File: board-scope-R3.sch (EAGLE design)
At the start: 71 parts, among them IC3 STM32F103C8T, J2 632723300011, U1 HD3SS3220IRNHT, U2 TUSB8020B, U3 FT600Q-T, U4 ICE40HX1K-VQ100VQ-100, U5 25F32006WSOI, U7 TPS54386, X1 30Mhz, X2 8Mhz

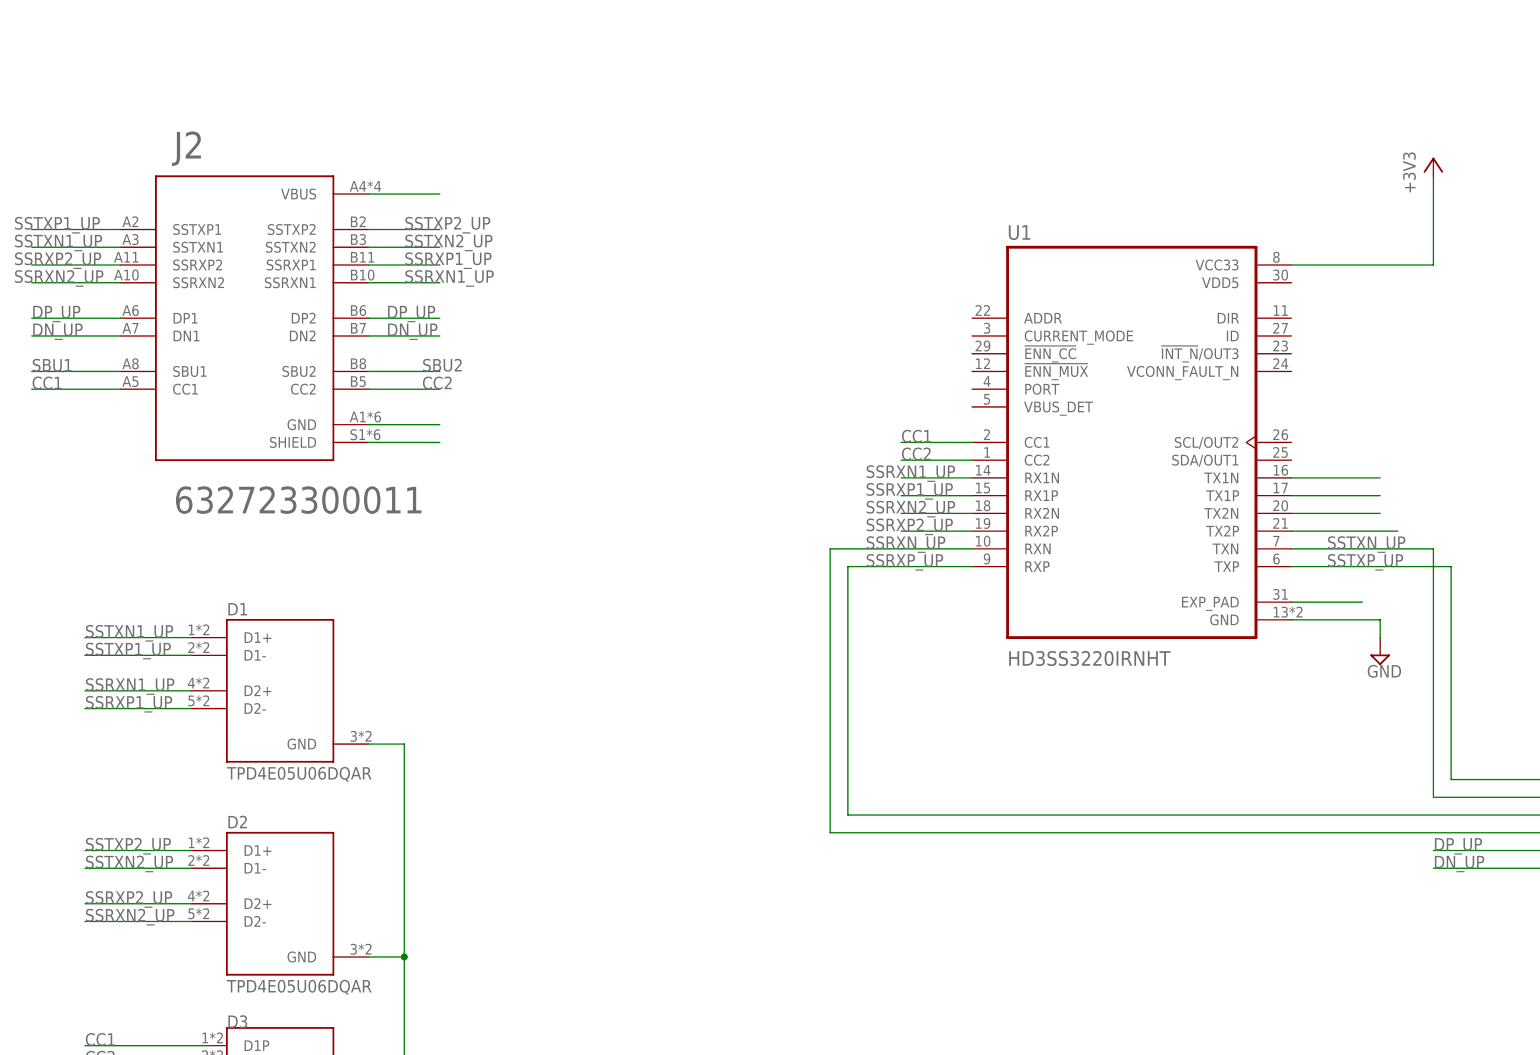
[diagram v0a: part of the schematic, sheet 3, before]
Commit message: routed power and usb
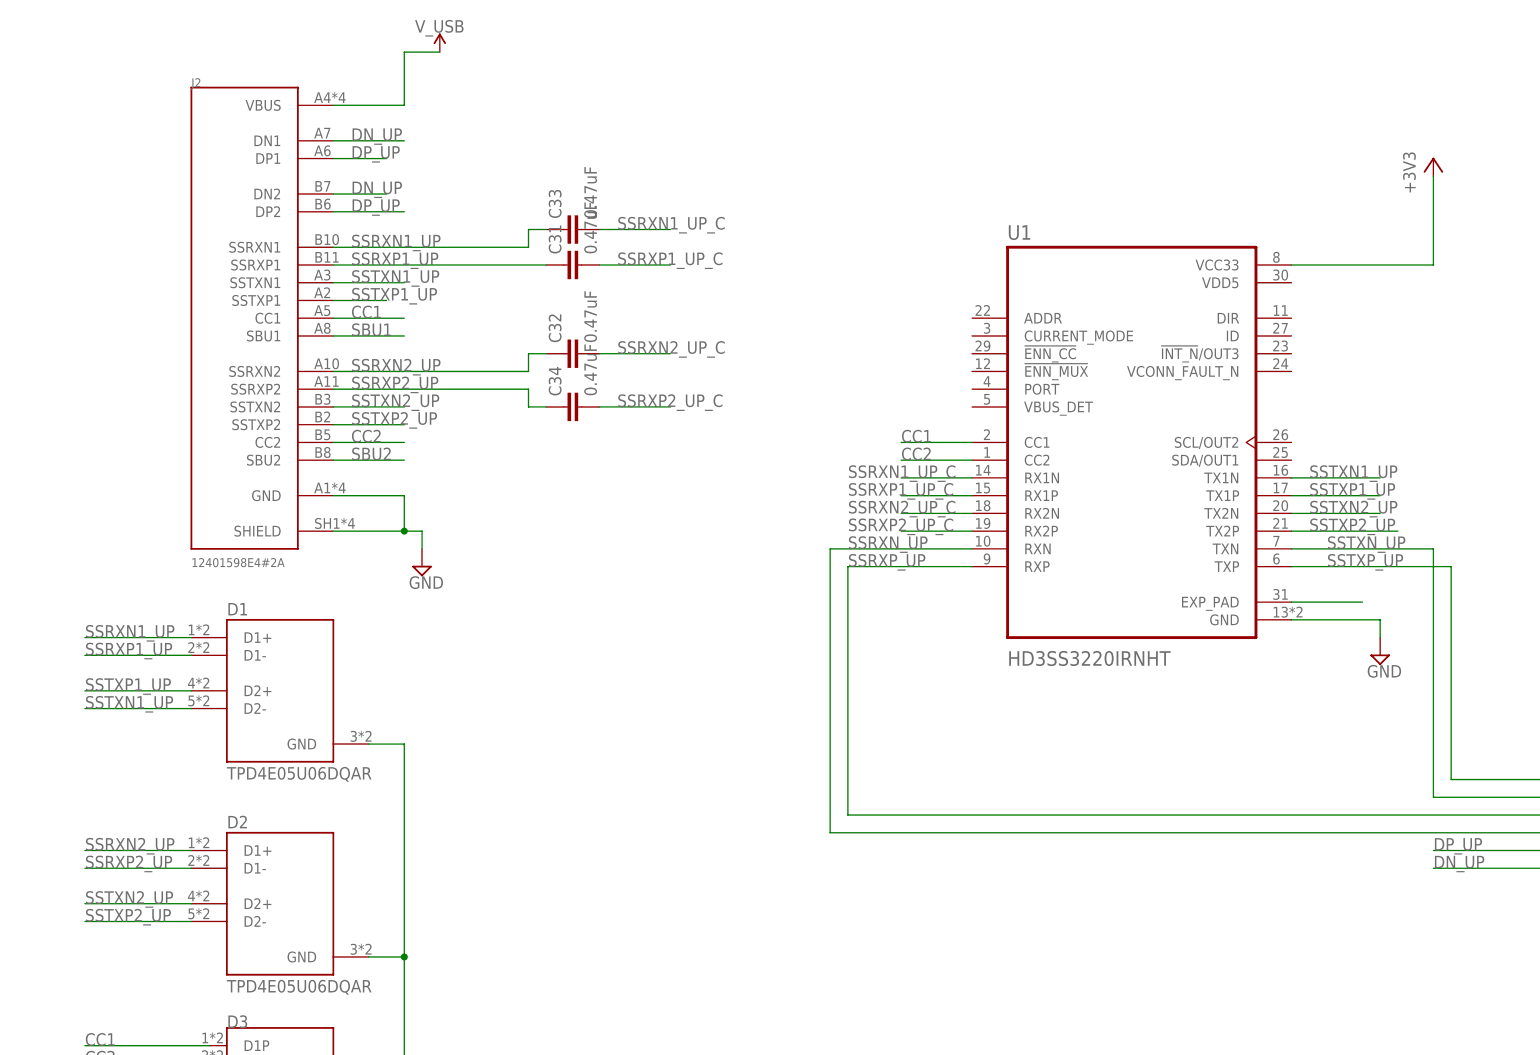
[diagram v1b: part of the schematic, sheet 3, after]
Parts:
- added C31, C32, C33, C34: 0.47uF, rcl:C-EUC0603K
- J2: value 632723300011 -> 12401598E4#2A; device 632723300011:632723300011 -> 12401598E4_2A:12401598E4#2A
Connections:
- removed net N$10: J2.SHIELD
- removed net N$11: J2.GND
- removed net N$12: U1.TX1N
- removed net N$13: U1.TX1P
- removed net N$14: U1.TX2N
- removed net N$15: U1.TX2P
- removed net N$9: J2.VBUS
- new net SSRXN1_UP_C: C33.2, U1.RX1N
- new net SSRXN2_UP_C: C32.2, U1.RX2N
- new net SSRXP1_UP_C: C31.2, U1.RX1P
- new net SSRXP2_UP_C: C34.2, U1.RX2P
- net GND: now also J2.GND, J2.SHIELD
- net SSRXN1_UP: now also C33.1, D1.D1+; no longer D1.D2+, U1.RX1N
- net SSRXN2_UP: now also C32.1, D2.D1+; no longer D2.D2-, U1.RX2N
- net SSRXP1_UP: now also C31.1, D1.D1-; no longer D1.D2-, U1.RX1P
- net SSRXP2_UP: now also C34.1, D2.D1-; no longer D2.D2+, U1.RX2P
- net SSTXN1_UP: now also D1.D2-, U1.TX1N; no longer D1.D1+
- net SSTXN2_UP: now also D2.D2+, U1.TX2N; no longer D2.D1-
- net SSTXP1_UP: now also D1.D2+, U1.TX1P; no longer D1.D1-
- net SSTXP2_UP: now also D2.D2-, U1.TX2P; no longer D2.D1+
- net V_USB: now also J2.VBUS
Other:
- moved on the sheet: J2

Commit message: saving
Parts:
- removed C40, C41, C42, C43, C44, C45, C46, C47: 0.1uF, rcl:C-EUC0603K
- added B10, B11, B12, B13, B14, B15, B8, B9: (no value), SparkFun-LED:LED0603
- added C600, C610, C620, C630, C650, C651: 1uF, rcl:C-EUC0603K
- added C601, C611, C621, C631, C652, C653: 0.1uF, rcl:C-EUC0603K
- added C602, C603, C612, C613, C622, C623, C632, C633, C654, C655, C656: 10nF, rcl:C-EUC0603K
- added D4: 1A/23V/620mV, SparkFun-DiscreteSemi:DIODE-SCHOTTKY-BAT20J
- added R11: 330, mylib:CTS742C163
- added R7, R8: 10k, rcl:R-US_R0603
- added S1, S3: (no value), mylib:MOMENTARY-SWITCH-SPST-2-SMD-5.2MM
- U4: value ICE40HX1K-VQ100VQ-100 -> ICE40HX1K-VQ100; device ice40hx1k-vq100:ICE40HX1K-VQ100VQ-100 -> mylib:ICE40HX1K-VQ100
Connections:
- removed net ICE40_VCCIO1: C44.1, C45.1, C46.1, C47.1
- new net BM_MISO: IC3MCU.PB4, U4.IOB_45_SDI, U5.MISO
- new net BM_MOSI: IC3MCU.PB5, U4.IOB_44_SDO, U5.MOSI
- new net BM_SCK: IC3MCU.PB3, U4.IOB_46_SCK, U5.SCK
- new net BTN_A: S1.3
- new net BTN_B: S3.3
- new net ICE_CDONE: IC3MCU.PB6
- new net ICE_CRESET: IC3MCU.PB7
- new net ICE_SS: IC3MCU.PB8, U4.IOB_47_SS, U5.CS
- new net LED0: R11.9
- new net LED1: R11.10
- new net LED2: R11.11
- new net LED3: R11.12
- new net LED4: R11.13
- new net LED5: R11.14
- new net LED6: R11.15
- new net LED7: R11.16
- new net N$1: D4.C, U4.VPP_2V5
- new net N$13: B8.A, R11.1
- new net N$14: B9.A, R11.2
- new net N$15: B10.A, R11.3
- new net N$2: IC3MCU.PB9
- new net N$20: B11.A, R11.4
- new net N$21: B12.A, R11.5
- new net N$3: IC3MCU.BOOT0, R8.2
- new net N$34: B13.A, R11.6
- new net N$35: B14.A, R11.7
- new net N$36: B15.A, R11.8
- net +3V3: now also D4.A, R7.2, U4.VCCIO_0, U4.VCCIO_1, U4.VCCIO_2, U4.VCCIO_3, U4.VCC_SPI, U5.VCC
- net BM_RST: now also R7.1
- net BM_TDO: no longer IC3MCU.PB3
- net GND: now also B10.C, B11.C, B12.C, B13.C, B14.C, B15.C, B8.C, B9.C, C600.2, C601.2, C602.2, C603.2, C610.2, C611.2, C612.2, C613.2, C620.2, C621.2, C622.2, C623.2, C630.2, C631.2, C632.2, C633.2, C650.2, C651.2, C652.2, C653.2, C654.2, C655.2, C656.2, R8.1, S1.1, S3.1, U4.GND, U5.GND; no longer C40.2, C41.2, C42.2, C43.2, C44.2, C45.2, C46.2, C47.2, IC3MCU.BOOT0
- net ICE40_VCCIO0: now also C600.1, C601.1, C602.1, C603.1, C610.1, C611.1, C612.1, C613.1, C620.1, C621.1, C622.1, C623.1, C630.1, C631.1, C632.1, C633.1, C650.1, C651.1, C652.1, C653.1, C654.1, C655.1, C656.1; no longer C40.1, C41.1, C42.1, C43.1
- net VCCINT: now also U4.VCC

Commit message: saving progress
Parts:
- added B1, B2: (no value), SparkFun-LED:LED0603
- added C35: 47uF, rcl:C-EUC0603K
- added C36, C37: 18pF, rcl:C-EUC0603K
- added R12, R18: 900k, rcl:R-US_R0603
- added R13, R17: 4.7k, rcl:R-US_R0603
- added R14, R15, R16: 200k, rcl:R-US_R0603
- added R19, R20: 330, rcl:R-US_R0603
- added X3: 24Mhz, SparkFun-Clocks:CRYSTALSMD-5X3.2-4PAD
- added Y1: OSCILLATORSMD-5X3, SparkFun-Clocks:OSCILLATORSMD-5X3
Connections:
- removed net ICE40_VCCIO0: C600.1, C601.1, C602.1, C603.1, C610.1, C611.1, C612.1, C613.1, C620.1, C621.1, C622.1, C623.1, C630.1, C631.1, C632.1, C633.1, C650.1, C651.1, C652.1, C653.1, C654.1, C655.1, C656.1
- new net ICE_CLK: U4.IOB_35_GBIN5, Y1.OUT
- new net N$10: R15.2, U1.ID
- new net N$11: U1.ADDR
- new net N$12: U1.CURRENT_MODE
- new net N$22: R17.1, U1.!ENN_CC
- new net N$23: R14.2, U1.DIR
- new net N$24: U1.SCL/OUT2
- new net N$37: R16.2, U1.!INT_N!/OUT3
- new net N$38: U1.VCONN_FAULT_N
- new net N$39: U1.SDA/OUT1
- new net N$4: R12.1, U1.VBUS_DET
- new net N$40: U2.SDA/SMBDAT
- new net N$41: U2.SMBUSZ/SS_DN2
- new net N$42: U2.FULLPWRMGMTZ/SMBA1/SS_UP
- new net N$43: U2.PWRCTL_POL/SS_DN1
- new net N$44: U2.GANGED/SMBA2/HS_UP
- new net N$45: R18.2, U2.TEST
- new net N$46: U2.PWRCTL2/BATEN2
- new net N$47: U2.OVERCUR2Z
- new net N$48: U2.PWRCTL1/BATEN1
- new net N$49: U2.OVERCUR1Z
- new net N$50: U2.USB_SSRXM_DN1
- new net N$51: U2.USB_SSRXP_DN1
- new net N$52: U2.USB_SSTXM_DN1
- new net N$53: U2.USB_SSTXP_DN1
- new net N$54: C36.1, U2.XI, X3.1
- new net N$55: C37.1, U2.XO, X3.2
- new net N$56: U$1.B15
- new net N$57: B1.C, R19.2
- new net N$58: U$1.B7
- new net N$59: U4.IOR_59
- new net N$60: U$1.B14
- new net N$61: B2.C, R20.2
- new net N$70: U4.IOL_6A
- new net N$9: R13.2, U1.PORT
- net +3V3: now also B2.A, C600.1, C601.1, C602.1, C603.1, C610.1, C611.1, C612.1, C613.1, C620.1, C621.1, C622.1, C623.1, C630.1, C631.1, C632.1, C633.1, U$1.A1, U$1.B1, U2.VDD33@1, U2.VDD33@2, U2.VDD33@3, U2.VDD33@4, U2.VDD33@5, U2.VDD33@6, U2.VDD33@7, U2.VDD33@8, Y1.EN, Y1.VCC
- net BM_LED0: now also B1.A
- net BM_MISO: now also U$1.A13
- net BM_MOSI: now also U$1.A14
- net BM_RST: now also U$1.B13
- net BM_RX: now also U$1.A17, U4.IOR_57
- net BM_SCK: now also U$1.A15
- net BM_TCK: now also U$1.B16
- net BM_TMS: now also U$1.B17
- net BM_TRGT_RST: now also U4.IOR_55
- net BM_TRGT_TCK: now also U4.IOR_52
- net BM_TRGT_TDI: now also U4.IOR_56
- net BM_TRGT_TDO: now also U4.IOR_54
- net BM_TRGT_TMS: now also U4.IOR_53
- net BM_TX: now also U$1.A16, U4.IOR_58
- net FT_D0: now also U4.IOL_5B
- net FT_D1: now also U4.IOL_5A
- net FT_D2: now also U4.IOL_3B
- net FT_D3: now also U4.IOL_3A
- net FT_D4: now also U4.IOL_2B
- net FT_D5: now also U4.IOL_2A
- net FT_D6: now also U4.IOL_1B
- net FT_D7: now also U4.IOL_1A
- net GND: now also C35.2, C36.2, C37.2, R13.1, R17.2, R18.1, R19.1, R20.1, U$1.A11, U$1.A12, U$1.B11, U$1.B12, U1.!ENN_MUX, U1.EXP_PAD, U2.PAD, Y1.GND
- net ICE_CDONE: now also U$1.B8, U4.CDONE
- net ICE_CRESET: now also U$1.B9, U4.CRESET_B
- net ICE_SS: now also U$1.B10
- net N$18: now also U2.SCL/SMBCLK; no longer U1.EXP_PAD
- net VCCINT: now also C650.1, C651.1, C652.1, C653.1, C654.1, C655.1, C656.1, U2.VDD, U2.VDD@1, U2.VDD@2, U2.VDD@3, U2.VDD@4
- net V_USB: now also C35.1, R12.2, R14.1, R15.1, R16.1, U1.VDD5
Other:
- note added: "J-TAG interface"
- note added: "x"
- note removed: "Do these get swapped?!"
- moved on the sheet: U5

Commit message: saving more..
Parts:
- removed S1, S3: (no value), mylib:MOMENTARY-SWITCH-SPST-2-SMD-5.2MM
- added C38: 1uF, rcl:C-EUC0603K
- added R21: 90.9k, rcl:R-US_R0603
- added R22, R25, R26: 10k, rcl:R-US_R0603
- added R23: 9.09k 1%, rcl:R-US_R0603
- added R24: (no value), rcl:R-US_R0603
- added S2: (no value), mylib:MOMENTARY-SWITCH-SPST-2-SMD-5.2MM
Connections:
- removed net BTN_A: S1.3
- removed net BTN_B: S3.3
- removed net LED0: R11.9
- removed net LED1: R11.10
- removed net LED2: R11.11
- removed net LED3: R11.12
- removed net LED4: R11.13
- removed net LED5: R11.14
- removed net LED6: R11.15
- removed net LED7: R11.16
- removed net N$59: U4.IOR_59
- removed net N$70: U4.IOL_6A
- new net CH01: U$3.4, U4.IOR_59
- new net CH02: U$3.6, U4.IOR_63
- new net CH03: U$3.8, U4.IOR_65
- new net CH04: U$3.10, U4.IOR_68
- new net CH05: U$3.12, U4.IOR_70
- new net CH06: U$3.14, U4.IOR_72
- new net CH07: U$3.3, U4.IOR_61_GBIN2
- new net CH08: U$3.5, U4.IOR_64
- new net CH09: U$3.7, U4.IOR_67
- new net CH10: U$3.9, U4.IOR_69
- new net CH11: U$3.11, U4.IOR_71
- new net CH12: U$3.13, U4.IOT_73
- new net CH13: U$4.4, U4.IOT_74
- new net CH14: U$4.6, U4.IOT_77
- new net CH15: U$4.8, U4.IOT_80
- new net CH16: U$4.10, U4.IOT_82
- new net CH17: U$4.12, U4.IOT_85_GBIN0
- new net CH18: U$4.14, U4.IOT_87
- new net CH19: U$4.16, U4.IOT_89
- new net CH20: U$4.18, U4.IOT_91
- new net CH21: U$4.20, U4.IOT_95
- new net CH22: U$4.22, U4.IOB_42_CBSEL0
- new net CH23: U$4.3, U4.IOT_75
- new net CH24: U$4.5, U4.IOT_78
- new net CH25: R11.16, U$4.7, U4.IOT_79
- new net CH26: R11.15, U$4.9, U4.IOT_81
- new net CH27: R11.14, U$4.11, U4.IOT_84_GBIN1
- new net CH28: R11.13, U$4.13, U4.IOT_86
- new net CH29: R11.12, U$4.15, U4.IOT_88
- new net CH30: R11.11, U$4.17, U4.IOT_90
- new net CH31: R11.10, U$4.19, U4.IOT_93
- new net CH32: R11.9, U$4.21, U4.IOL_1A
- new net ICE_RESET: R24.1, S2.3, U4.IOR_60_GBIN3
- new net N$62: C38.1, U2.GRSTZ
- new net N$63: R21.1, R22.2, U2.USB_VBUS
- new net N$64: R23.2, U2.USB_R1
- new net N$65: U4.IOB_43_CBSEL1
- net +3V3: now also R25.2, R26.2, U$3.15, U$3.16
- net FT_BE0: now also U4.IOB_41
- net FT_BE1: now also U4.IOB_37
- net FT_CLK: now also U4.IOL_6B_GBIN7
- net FT_D0: now also U4.IOL_12B; no longer U4.IOL_5B
- net FT_D1: now also U4.IOL_12A; no longer U4.IOL_5A
- net FT_D10: now also U4.IOL_5A
- net FT_D11: now also U4.IOL_3B
- net FT_D12: now also U4.IOL_3A
- net FT_D13: now also U4.IOL_2B
- net FT_D14: now also U4.IOL_2A
- net FT_D15: now also U4.IOL_1B
- net FT_D2: now also U4.IOL_10B; no longer U4.IOL_3B
- net FT_D3: now also U4.IOL_10A; no longer U4.IOL_3A
- net FT_D4: now also U4.IOL_8B; no longer U4.IOL_2B
- net FT_D5: now also U4.IOL_8A; no longer U4.IOL_2A
- net FT_D6: now also U4.IOL_7B; no longer U4.IOL_1B
- net FT_D7: now also U4.IOL_7A_GBIN6; no longer U4.IOL_1A
- net FT_D8: now also U4.IOL_6A
- net FT_D9: now also U4.IOL_5B
- net FT_GPIO_0: now also U4.IOB_27
- net FT_GPIO_1: now also U4.IOB_26
- net FT_OE: now also U4.IOB_28
- net FT_RD: now also U4.IOB_29
- net FT_RST: now also R26.1
- net FT_RXF: now also U4.IOB_36_GBIN4
- net FT_SIWU: now also R25.1
- net FT_TXE: now also U4.IOB_34
- net FT_WR: now also U4.IOB_30
- net GND: now also C38.2, R22.1, R23.1, S2.1, U$3.1, U$3.2, U$4.1, U$4.2; no longer S1.1, S3.1
- net V_USB: now also R21.2, U$4.23, U$4.24
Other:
- moved on the sheet: D4, U$3, U$4, U4, Y1

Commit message: almost done routing
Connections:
- net BM_TDI: no longer IC3MCU.PA15
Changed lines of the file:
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@@
 <net name="BM_TDI" class="0">
-<segment>
-<pinref part="IC3" gate="MCU" pin="PA15"/>
-<wire x1="132.08" y1="154.94" x2="148.59" y2="154.94" width="0.1524" layer="91"/>
-</segment>
 <segment>
 <pinref part="U$2" gate="G$1" pin="TDI"/>
